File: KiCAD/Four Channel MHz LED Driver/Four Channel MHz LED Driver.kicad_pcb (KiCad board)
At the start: 2 copper layers, 100 x 100 mm, 92 parts, among them J1 Barrel_Jack_Switch, J10 Conn_01x24_Female, J2 Conn_01x02_Female, J3 8P8C_Shielded_x4, J4 Conn_01x03_Male, J5 Conn_01x03_Female, J6 Conn_01x08_Female, J7 Conn_01x03_Female, J8 Conn_01x05_Female, J9 Conn_01x24_Female, M1 Fan_4pin, Q1 SUM70060E, SW1 Pushbutton_with_LED, SW2 Pushbutton_with_LED, SW3 Pushbutton_with_LED, SW4 Pushbutton_with_LED, SW5 SW_SPDT, U1 12V boost, U10 ASSR-1218, U11 ASSR-1218, U12 Teensy3.6, U2 SN74LV4T125PWR, U3 DPBW06F-05, U4 TMUX1204DGSR, U5 BDJ0GA5WEFJ-E2, U6 ADP7182AUJZ-1.8-R7, U7 LT6200CS8-10, U8 ASSR-1218, U9 ASSR-1218

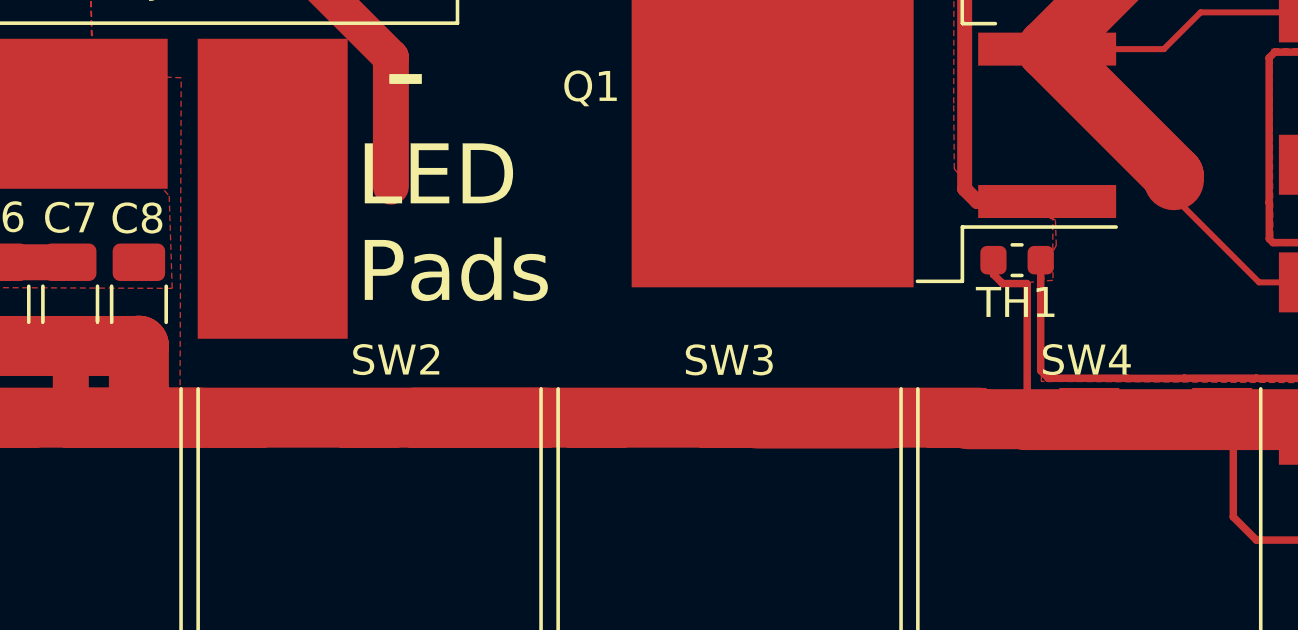
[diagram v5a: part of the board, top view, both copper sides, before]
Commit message: one more courtyard resolved
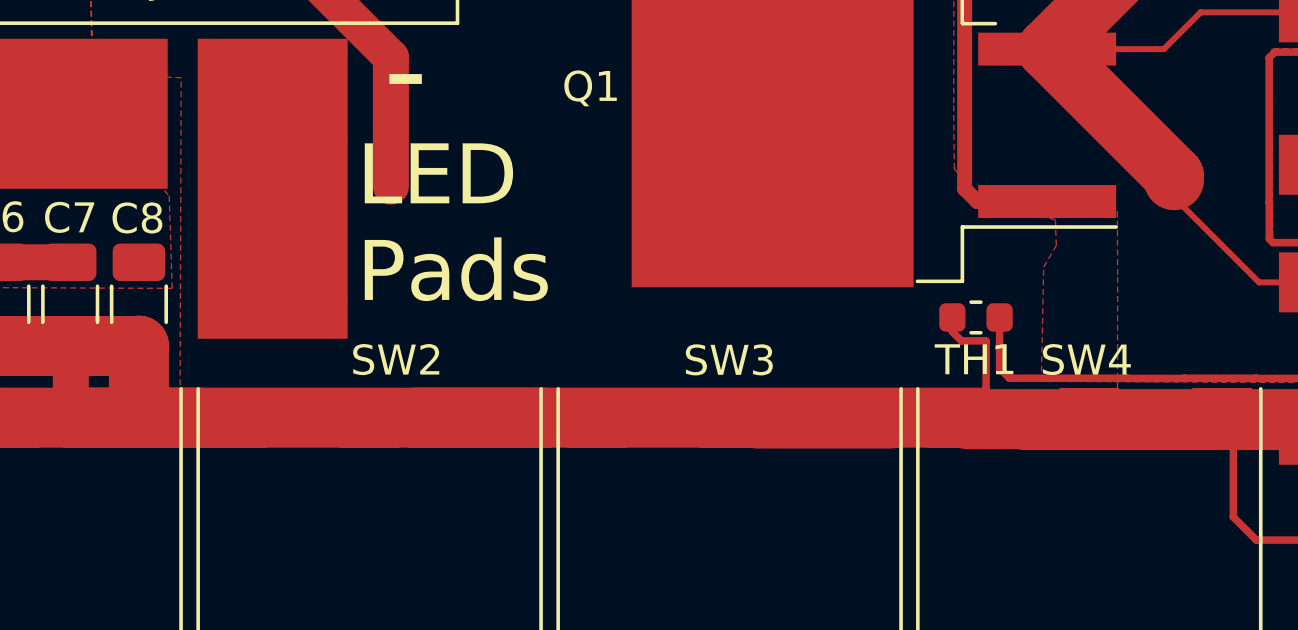
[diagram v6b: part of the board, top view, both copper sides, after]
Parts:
- moved TH1 2.35 mm to (98.9, 98.9)
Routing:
- net GND: track 1150.5 -> 1149.7 mm
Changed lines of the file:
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@@
     (thickness 1.6)
     (drawings 18)
-    (tracks 1936)
+    (tracks 1938)
     (zones 0)
     (modules 92)
@@
   )
   (module Resistor_SMD:R_0603_1608Metric (layer F.Cu)
-    (at 100.2825 96.99 180)
+    (at 98.9125 98.9 180)
     (descr "Resistor SMD 0603 (1608 Metric), square (rectangular) end terminal, IPC_7351 nominal, (Body size source: http://www.tortai-tech.com/upload/download/2011102023233369053.pdf), generated with kicad-footprint-generator")
     (tags resistor)
@@
   (segment (start 38.35 33) (end 38.23 33) (width 2) (layer F.Cu) (net 2))
   (segment (start 38.23 33) (end 38.22501 33.00499) (width 2) (layer F.Cu) (net 2))
-  (segment (start 99.495 96.99) (end 99.495 97.465) (width 0.25) (layer F.Cu) (net 2))
-  (segment (start 99.8 97.77) (end 100.606006 97.77) (width 0.25) (layer F.Cu) (net 2))
-  (segment (start 99.495 97.465) (end 99.8 97.77) (width 0.25) (layer F.Cu) (net 2))
-  (segment (start 100.61999 97.783984) (end 100.61999 101.73999) (width 0.25) (layer F.Cu) (net 2))
-  (segment (start 100.606006 97.77) (end 100.61999 97.783984) (width 0.25) (layer F.Cu) (net 2))
   (segment (start 100.06998 102.29) (end 98.63 102.29) (width 0.25) (layer F.Cu) (net 2))
   (segment (start 100.61999 101.73999) (end 100.06998 102.29) (width 0.25) (layer F.Cu) (net 2))
@@
   (segment (start 96.08 67.66) (end 96.13 67.71) (width 0.5) (layer F.Cu) (net 2))
   (segment (start 93.72 67.66) (end 96.08 67.66) (width 0.5) (layer F.Cu) (net 2))
+  (segment (start 98.125 102.115) (end 98.26 102.25) (width 0.25) (layer F.Cu) (net 2))
+  (segment (start 98.43 99.68) (end 99.236006 99.68) (width 0.25) (layer F.Cu) (net 2))
+  (segment (start 98.125 98.9) (end 98.125 99.375) (width 0.25) (layer F.Cu) (net 2))
+  (segment (start 98.125 99.375) (end 98.43 99.68) (width 0.25) (layer F.Cu) (net 2))
+  (segment (start 99.24999 101.26001) (end 98.26 102.25) (width 0.25) (layer F.Cu) (net 2))
+  (segment (start 99.24999 99.693984) (end 99.24999 101.26001) (width 0.25) (layer F.Cu) (net 2))
+  (segment (start 99.236006 99.68) (end 99.24999 99.693984) (width 0.25) (layer F.Cu) (net 2))
   (segment (start 45.34 54.5) (end 43.92 53.08) (width 0.25) (layer F.Cu) (net 3))
   (segment (start 45.34 56.08) (end 45.34 54.5) (width 0.25) (layer F.Cu) (net 3))
@@
   (segment (start 102.25 46.408502) (end 104.440009 48.598511) (width 0.2) (layer F.Cu) (net 40))
   (segment (start 102.25 43.39) (end 102.25 46.408502) (width 0.2) (layer F.Cu) (net 40))
-  (segment (start 101.07 96.99) (end 101.07 97.597584) (width 0.25) (layer F.Cu) (net 40))
-  (segment (start 101.07 97.597584) (end 101.07 100.67) (width 0.25) (layer F.Cu) (net 40))
   (segment (start 101.424998 100.93) (end 101.429999 100.924999) (width 0.25) (layer F.Cu) (net 40))
-  (segment (start 101.07 100.67) (end 101.33 100.93) (width 0.25) (layer F.Cu) (net 40))
   (segment (start 101.33 100.93) (end 101.424998 100.93) (width 0.25) (layer F.Cu) (net 40))
   (segment (start 103.955002 100.93) (end 105.854998 100.93) (width 0.25) (layer F.Cu) (net 40))
@@
   (segment (start 105.149794 65.119794) (end 105.105592 65.075592) (width 0.2) (layer F.Cu) (net 40))
   (segment (start 103.802899 63.767101) (end 103.807899 63.772101) (width 0.2) (layer F.Cu) (net 40))
+  (segment (start 99.7 98.9) (end 99.7 100.6) (width 0.25) (layer F.Cu) (net 40))
+  (segment (start 100.024999 100.924999) (end 101.429999 100.924999) (width 0.25) (layer F.Cu) (net 40))
+  (segment (start 99.7 100.6) (end 100.024999 100.924999) (width 0.25) (layer F.Cu) (net 40))
   (segment (start 125.68 121.695) (end 125.68 122.52) (width 0.25) (layer F.Cu) (net 41))
   (segment (start 132.73 45.222602) (end 132.73 43.39) (width 0.2) (layer F.Cu) (net 41))
@@
         (xy 93.3 75.87) (xy 94.06 76.52) (xy 96.41 76.54) (xy 97.11 77.22) (xy 97.76 77.84)
         (xy 97.79 80.07) (xy 97.78 81.3) (xy 96.02 83.9) (xy 98.62 86.39) (xy 98.53 94.65)
-        (xy 99.22 95.26) (xy 101.47 95.47) (xy 101.48 97.66) (xy 100.68 97.73) (xy 100.71 101.82)
-        (xy 72.38 101.8) (xy 72.42 90.91) (xy 69.45 90.79) (xy 69.33 83.85) (xy 69.38 74.7)
-        (xy 60.9 74.64) (xy 59.76 74.61) (xy 59.94 73.73) (xy 53.42 73.76) (xy 51.72 69.92)
+        (xy 99.22 95.26) (xy 103.625 95.355) (xy 103.635 97.545) (xy 103.63 101.74) (xy 72.38 101.8)
+        (xy 72.42 90.91) (xy 69.45 90.79) (xy 69.33 83.85) (xy 69.38 74.7) (xy 60.9 74.64)
+        (xy 59.76 74.61) (xy 59.94 73.73) (xy 53.42 73.76) (xy 51.72 69.92)
       )
     )

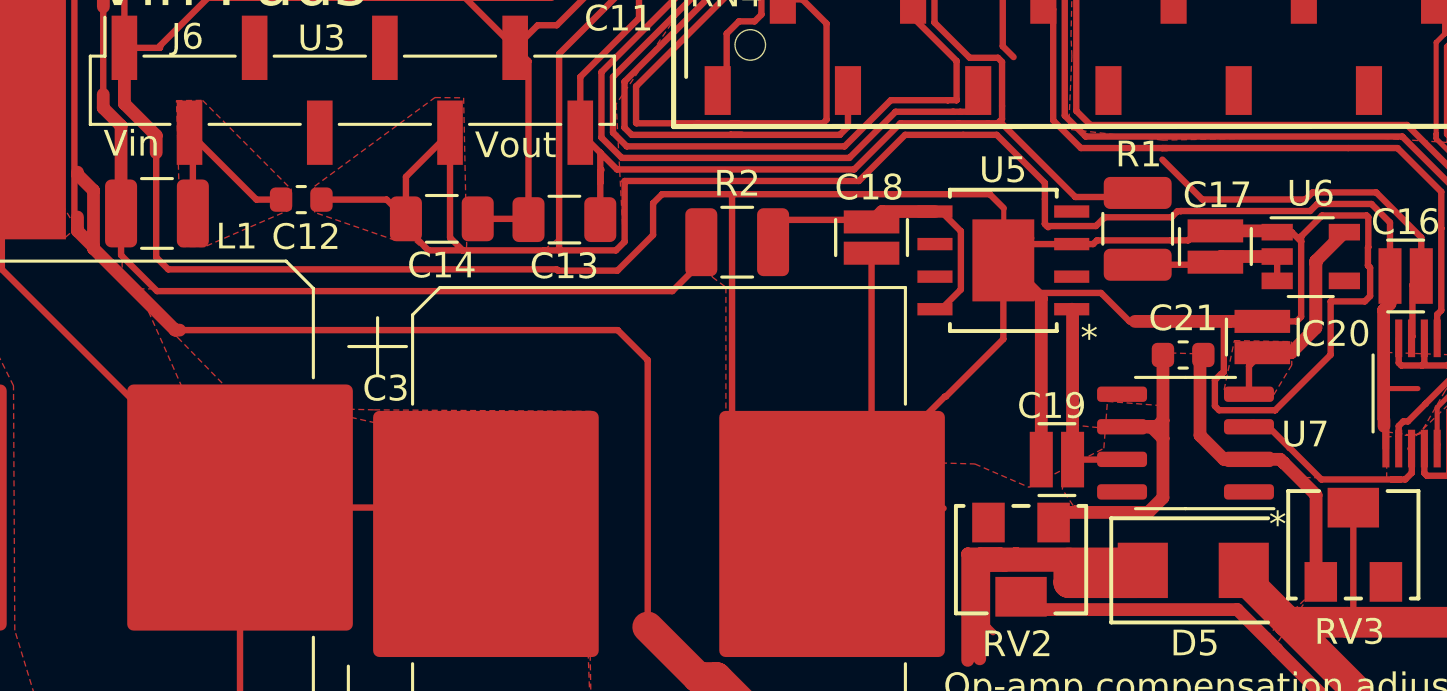
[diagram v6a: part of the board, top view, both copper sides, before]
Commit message: Improved LDO bypass
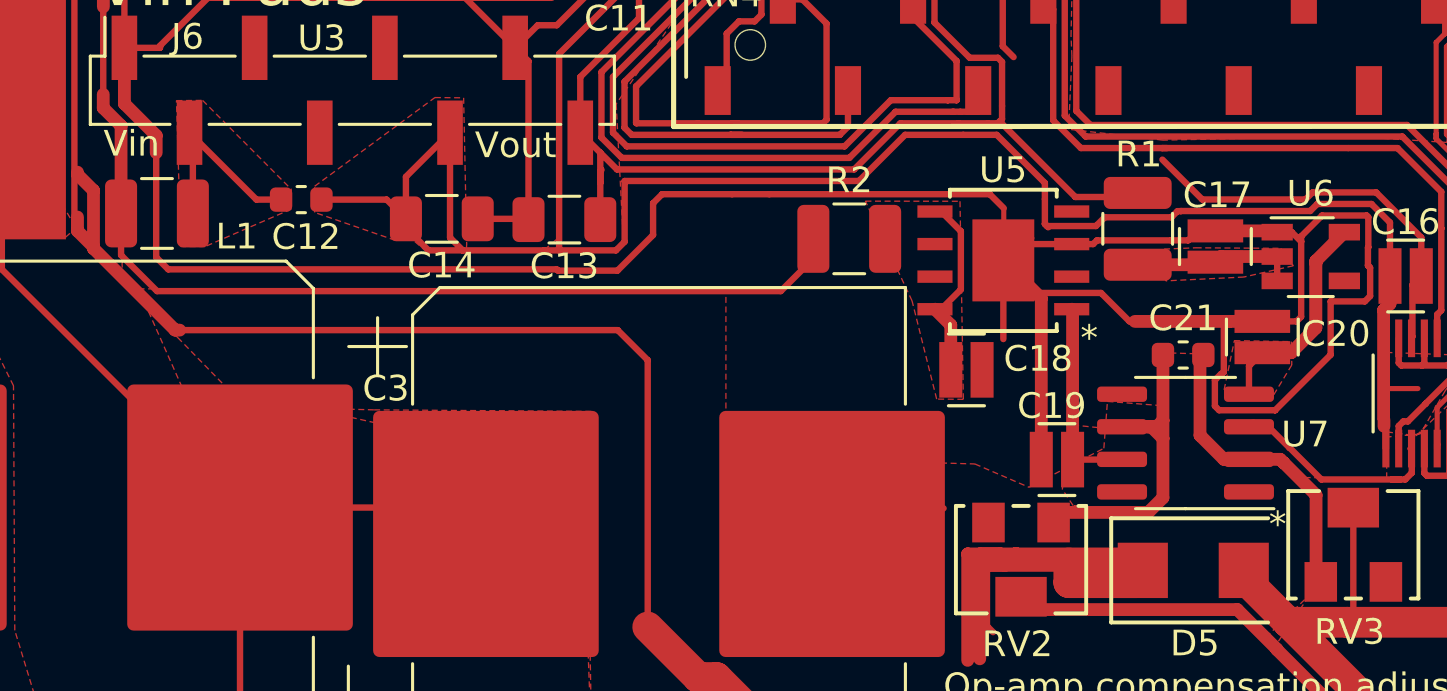
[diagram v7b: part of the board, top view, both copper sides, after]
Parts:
- moved C18 6.35 mm to (84.0, 73.1), turned to 0 degrees
- moved R2 4.37 mm to (79.4, 68.0)
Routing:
- net GND: track 1149.7 -> 1125.0 mm
- net /12V: track 67.3 -> 71.9 mm
- net Net-(C18-Pad1): track 11.5 -> 7.55 mm
- net Net-(C17-Pad1): track 6.06 -> 9.43 mm
- added copper zone on F.Cu, net Net-(C17-Pad1)
- added copper zone on F.Cu, net Net-(C18-Pad1)
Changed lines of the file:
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@@
     (thickness 1.6)
     (drawings 18)
-    (tracks 1938)
+    (tracks 1936)
     (zones 0)
     (modules 92)
@@
   )
   (module "Custom Footprints:0508_Capacitor" (layer F.Cu)
-    (at 80.31 67.92 270)
-    (fp_text reference C18 (at -1.95 0.09 180) (layer F.SilkS)
+    (at 84.01 73.08)
+    (fp_text reference C18 (at 2.8 -0.43) (layer F.SilkS)
       (effects (font (size 1 1) (thickness 0.15)))
     )
-    (fp_text value 2.2uF (at 1.79 1.81 90) (layer F.Fab)
+    (fp_text value 2.2uF (at 1.79 1.81) (layer F.Fab)
       (effects (font (size 0.393701 0.393701) (thickness 0.015)))
     )
@@
     (fp_line (start 0.7 -1.08) (end -0.7 -1.08) (layer F.Fab) (width 0.127))
     (fp_line (start 0.7 1.08) (end -0.7 1.08) (layer F.Fab) (width 0.127))
-    (pad 1 smd rect (at -0.61 0 270) (size 0.9 2.17) (layers F.Cu F.Paste F.Mask)
+    (pad 1 smd rect (at -0.61 0) (size 0.9 2.17) (layers F.Cu F.Paste F.Mask)
       (net 85 "Net-(C18-Pad1)"))
-    (pad 2 smd rect (at 0.61 0 270) (size 0.9 2.17) (layers F.Cu F.Paste F.Mask)
+    (pad 2 smd rect (at 0.61 0) (size 0.9 2.17) (layers F.Cu F.Paste F.Mask)
       (net 2 GND))
     (model "C:/Users/Ben/Documents/GitHub/Four_Channel_MHz_LED_Driver/KiCAD/Custom Parts/STEP/0508 capacitor.STEP"
@@
   )
   (module Resistor_SMD:R_1210_3225Metric (layer F.Cu)
-    (at 75.07 68.1)
+    (at 79.44 67.97)
     (descr "Resistor SMD 1210 (3225 Metric), square (rectangular) end terminal, IPC_7351 nominal, (Body size source: http://www.tortai-tech.com/upload/download/2011102023233369053.pdf), generated with kicad-footprint-generator")
     (tags resistor)
@@
   (segment (start 59.11 58.57) (end 64.46 58.57) (width 0.25) (layer F.Cu) (net 2))
   (segment (start 82.77221 78.48) (end 78.81 78.48) (width 0.25) (layer F.Cu) (net 2))
-  (segment (start 83.17 74.12) (end 78.81 78.48) (width 0.25) (layer F.Cu) (net 2))
   (segment (start 96.885 71.19) (end 95.55 71.19) (width 0.25) (layer F.Cu) (net 2))
   (segment (start 97.065001 71.009999) (end 96.885 71.19) (width 0.25) (layer F.Cu) (net 2))
@@
   (segment (start 72.13998 66.23002) (end 74.87 66.23002) (width 0.25) (layer F.Cu) (net 2))
   (segment (start 74.87 75.58) (end 78.77 79.48) (width 0.25) (layer F.Cu) (net 2))
-  (segment (start 74.87 66.23002) (end 74.87 75.58) (width 0.25) (layer F.Cu) (net 2))
   (segment (start 80.31 77.94) (end 78.77 79.48) (width 0.25) (layer F.Cu) (net 2))
-  (segment (start 80.31 68.53) (end 80.31 77.94) (width 0.25) (layer F.Cu) (net 2))
-  (segment (start 83.17 74.12) (end 83.21 74.12) (width 0.25) (layer F.Cu) (net 2))
   (segment (start 85.45 71.88) (end 85.45 68.81) (width 0.25) (layer F.Cu) (net 2))
-  (segment (start 83.21 74.12) (end 85.45 71.88) (width 0.25) (layer F.Cu) (net 2))
   (segment (start 84.92222 66.23002) (end 85.467 66.7748) (width 0.25) (layer F.Cu) (net 2))
-  (segment (start 74.87 66.23002) (end 84.92222 66.23002) (width 0.25) (layer F.Cu) (net 2))
   (segment (start 101.75 69.42) (end 101.75 68.55) (width 0.25) (layer F.Cu) (net 2))
   (segment (start 77.155002 49.01) (end 77.175002 49.03) (width 0.25) (layer F.Cu) (net 2))
@@
   (segment (start 99.24999 99.693984) (end 99.24999 101.26001) (width 0.25) (layer F.Cu) (net 2))
   (segment (start 99.236006 99.68) (end 99.24999 99.693984) (width 0.25) (layer F.Cu) (net 2))
+  (segment (start 76.31998 77.02998) (end 78.77 79.48) (width 0.25) (layer F.Cu) (net 2))
+  (segment (start 76.31998 66.23002) (end 84.92222 66.23002) (width 0.25) (layer F.Cu) (net 2))
+  (segment (start 74.87 66.23002) (end 76.31998 66.23002) (width 0.25) (layer F.Cu) (net 2))
   (segment (start 45.34 54.5) (end 43.92 53.08) (width 0.25) (layer F.Cu) (net 3))
   (segment (start 45.34 56.08) (end 45.34 54.5) (width 0.25) (layer F.Cu) (net 3))
@@
   (segment (start 45.34 54.2) (end 45.34 56.08) (width 1.2) (layer F.Cu) (net 3))
   (segment (start 43.93 52.79) (end 45.34 54.2) (width 1.2) (layer F.Cu) (net 3))
-  (segment (start 73.64 68.91) (end 73.64 68.25) (width 0.25) (layer F.Cu) (net 3))
-  (segment (start 72.54 70.01) (end 73.64 68.91) (width 0.25) (layer F.Cu) (net 3))
-  (segment (start 52.44322 70.01) (end 72.54 70.01) (width 0.25) (layer F.Cu) (net 3))
-  (segment (start 51.04 66.98) (end 51.04 68.60678) (width 0.25) (layer F.Cu) (net 3))
-  (segment (start 51.04 68.60678) (end 52.44322 70.01) (width 0.25) (layer F.Cu) (net 3))
   (segment (start 50.35 58.999998) (end 50.344999 59.004999) (width 0.25) (layer F.Cu) (net 3))
   (segment (start 45.34 56.08) (end 45.75 56.08) (width 0.5) (layer F.Cu) (net 3))
@@
   (segment (start 45.34 56.08) (end 48.4 56.08) (width 0.5) (layer F.Cu) (net 3))
   (segment (start 48.4 56.08) (end 49.141812 56.08) (width 0.5) (layer F.Cu) (net 3))
+  (segment (start 78.04 68.74) (end 78.04 67.97) (width 0.25) (layer F.Cu) (net 3))
+  (segment (start 76.77 70.01) (end 78.04 68.74) (width 0.25) (layer F.Cu) (net 3))
+  (segment (start 52.44322 70.01) (end 76.77 70.01) (width 0.25) (layer F.Cu) (net 3))
+  (segment (start 51.04 66.98) (end 51.04 68.60678) (width 0.25) (layer F.Cu) (net 3))
+  (segment (start 51.04 68.60678) (end 52.44322 70.01) (width 0.25) (layer F.Cu) (net 3))
   (segment (start 69.73 64.61) (end 68.95 63.83) (width 0.25) (layer F.Cu) (net 4))
   (segment (start 69.73 65.33) (end 69.78 65.28) (width 0.25) (layer F.Cu) (net 4))
@@
   (segment (start 90.69 68.98) (end 93.3 68.98) (width 0.25) (layer F.Cu) (net 7))
   (segment (start 96.13 69.61) (end 96.13 68.66) (width 0.25) (layer F.Cu) (net 7))
-  (segment (start 93.94 68.66) (end 93.72 68.88) (width 0.5) (layer F.Cu) (net 7))
+  (segment (start 93.62 68.98) (end 93.72 68.88) (width 0.5) (layer F.Cu) (net 7))
+  (segment (start 90.69 68.98) (end 93.62 68.98) (width 0.5) (layer F.Cu) (net 7))
+  (segment (start 93.72 68.88) (end 94.02 68.88) (width 0.5) (layer F.Cu) (net 7))
   (segment (start 96.13 68.66) (end 93.94 68.66) (width 0.5) (layer F.Cu) (net 7))
+  (segment (start 93.94 68.66) (end 93.72 68.88) (width 0.5) (layer F.Cu) (net 7))
   (segment (start 90.07 76.58) (end 90.08 76.57) (width 0.25) (layer F.Cu) (net 8))
   (segment (start 88.15 76.58) (end 90.07 76.58) (width 0.25) (layer F.Cu) (net 8))
@@
   (segment (start 92.09 43.06) (end 94.2775 40.8725) (width 0.25) (layer F.Cu) (net 66))
   (segment (start 92.09 43.39) (end 92.09 43.06) (width 0.25) (layer F.Cu) (net 66))
-  (segment (start 80.23 67.23) (end 80.31 67.31) (width 0.25) (layer F.Cu) (net 85))
-  (segment (start 76.41 67.23) (end 80.23 67.23) (width 0.25) (layer F.Cu) (net 85))
   (segment (start 83.025102 70.715) (end 83.793801 69.946301) (width 0.25) (layer F.Cu) (net 85))
   (segment (start 82.783 70.715) (end 83.025102 70.715) (width 0.25) (layer F.Cu) (net 85))
@@
   (segment (start 101 56.15) (end 101.93 55.22) (width 0.2) (layer F.Cu) (net 81))
   (segment (start 88.99 56.15) (end 101 56.15) (width 0.2) (layer F.Cu) (net 81))
-  (segment (start 80.715 66.905) (end 80.31 67.31) (width 0.5) (layer F.Cu) (net 85))
-  (segment (start 82.783 66.905) (end 80.715 66.905) (width 0.5) (layer F.Cu) (net 85))
+  (segment (start 83.4 71.332) (end 82.783 70.715) (width 0.5) (layer F.Cu) (net 85))
+  (segment (start 83.4 73.08) (end 83.4 71.332) (width 0.5) (layer F.Cu) (net 85))
   (segment (start 84.62 52.899998) (end 84.62 55.86) (width 0.25) (layer F.Cu) (net 86))
   (segment (start 90.19 49.99) (end 87.529998 49.99) (width 0.25) (layer F.Cu) (net 86))
@@
     (polygon
       (pts
-        (xy 72.55 70.01) (xy 73.77 68.7) (xy 74.1 69.46) (xy 74.63 69.86) (xy 74.63 75.25)
-        (xy 78.53 75.17) (xy 81.62 77.36) (xy 82.27 76.69) (xy 84.34 76.75) (xy 86.45 77.66)
-        (xy 89.37 76.14) (xy 89.51 74.31) (xy 91.61 74.475) (xy 91.59 72.41) (xy 93.24 72.46)
-        (xy 93.3 75.87) (xy 94.06 76.52) (xy 96.41 76.54) (xy 97.11 77.22) (xy 97.76 77.84)
-        (xy 97.79 80.07) (xy 97.78 81.3) (xy 96.02 83.9) (xy 98.62 86.39) (xy 98.53 94.65)
-        (xy 99.22 95.26) (xy 103.625 95.355) (xy 103.635 97.545) (xy 103.63 101.74) (xy 72.38 101.8)
-        (xy 72.42 90.91) (xy 69.45 90.79) (xy 69.33 83.85) (xy 69.38 74.7) (xy 60.9 74.64)
-        (xy 59.76 74.61) (xy 59.94 73.73) (xy 53.42 73.76) (xy 51.72 69.92)
+        (xy 72.55 70.01) (xy 74.63 69.86) (xy 74.63 75.25) (xy 78.53 75.17) (xy 81.62 77.36)
+        (xy 82.27 76.69) (xy 84.34 76.75) (xy 86.45 77.66) (xy 89.37 76.14) (xy 89.51 74.31)
+        (xy 91.61 74.475) (xy 91.59 72.41) (xy 93.24 72.46) (xy 93.3 75.87) (xy 94.06 76.52)
+        (xy 96.41 76.54) (xy 97.11 77.22) (xy 97.76 77.84) (xy 97.79 80.07) (xy 97.78 81.3)
+        (xy 96.02 83.9) (xy 98.62 86.39) (xy 98.53 94.65) (xy 99.22 95.26) (xy 103.625 95.355)
+        (xy 103.635 97.545) (xy 103.63 101.74) (xy 72.38 101.8) (xy 72.42 90.91) (xy 69.45 90.79)
+        (xy 69.33 83.85) (xy 69.38 74.7) (xy 60.9 74.64) (xy 59.76 74.61) (xy 59.94 73.73)
+        (xy 53.42 73.76) (xy 51.72 69.92)
       )
     )
@@
       )
     )
+  )
+  (zone (net 85) (net_name "Net-(C18-Pad1)") (layer F.Cu) (hatch edge 0.508)
+    (priority 8)
+    (connect_pads yes (clearance 0.21))
+    (min_thickness 0.21)
+    (fill yes (arc_segments 32) (thermal_gap 0.508) (thermal_bridge_width 0.508))
+    (polygon
+      (pts
+        (xy 83.89 74.23) (xy 82.85 74.22) (xy 81.89 70.39) (xy 80.07 66.5) (xy 83.76 66.505)
+      )
+    )
+  )
+  (zone (net 7) (net_name "Net-(C17-Pad1)") (layer F.Cu) (hatch edge 0.508)
+    (priority 9)
+    (connect_pads yes (clearance 0.21))
+    (min_thickness 0.21)
+    (fill yes (arc_segments 32) (thermal_gap 0.508) (thermal_bridge_width 0.508))
+    (polygon
+      (pts
+        (xy 96.27 68.34) (xy 96.76 69.02) (xy 94.83 69.46) (xy 91.78 69.61) (xy 91.72 68.37)
+        (xy 92.95 68.32)
+      )
+    )
